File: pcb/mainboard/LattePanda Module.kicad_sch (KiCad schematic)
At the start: 12 parts, among them J1 Conn_01x03_Pin

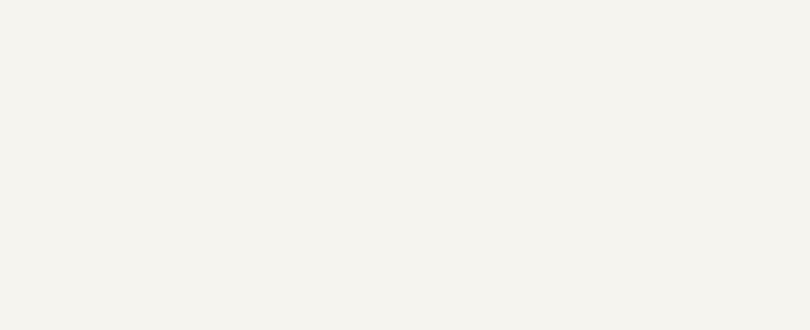
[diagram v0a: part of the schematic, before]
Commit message: most length matching almost done
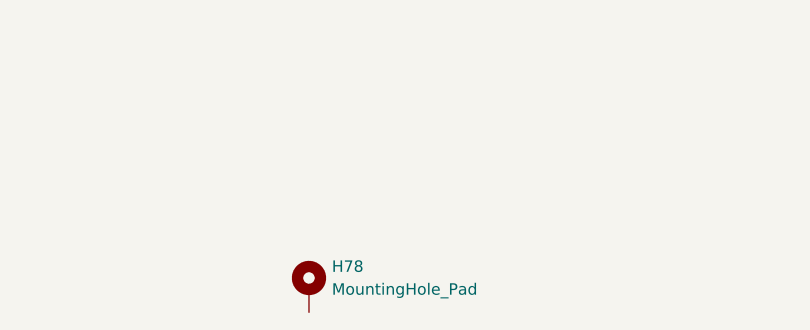
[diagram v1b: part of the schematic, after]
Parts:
- added H78: MountingHole_Pad, A_HDJ_Library:MountingHole_3mm_M2_Pad_TopOnly, symbol Mechanical:MountingHole_Pad
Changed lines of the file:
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@@
+	)
+	(symbol
+		(lib_name "MountingHole_Pad_1")
+		(lib_id "Mechanical:MountingHole_Pad")
+		(at 154.94 346.71 0)
+		(unit 1)
+		(exclude_from_sim no)
+		(in_bom no)
+		(on_board yes)
+		(dnp no)
+		(fields_autoplaced yes)
+		(property "Reference" "H78"
+			(at 157.48 344.1699 0)
+			(effects
+				(font
+					(size 1.27 1.27)
+				)
+				(justify left)
+			)
+		)
+		(property "Value" "MountingHole_Pad"
+			(at 157.48 346.7099 0)
+			(effects
+				(font
+					(size 1.27 1.27)
+				)
+				(justify left)
+			)
+		)
+		(property "Footprint" "A_HDJ_Library:MountingHole_3mm_M2_Pad_TopOnly"
+			(at 154.94 346.71 0)
+			(effects
+				(font
+					(size 1.27 1.27)
+				)
+				(hide yes)
+			)
+		)
+		(property "Datasheet" "~"
+			(at 154.94 346.71 0)
+			(effects
+				(font
+					(size 1.27 1.27)
+				)
+				(hide yes)
+			)
+		)
+		(property "Description" "Mounting Hole with connection"
+			(at 154.94 346.71 0)
+			(effects
+				(font
+					(size 1.27 1.27)
+				)
+				(hide yes)
+			)
+		)
+		(pin "1"
+		)
+		(instances
+			(project ""
+				(path "/2a6d114a-7fd7-4207-b5f7-4ea9c34f36aa/6eee02c2-78c9-4e83-9ccf-e0f7690b57bf"
+					(reference "H78")
+					(unit 1)
+				)
+			)
+		)
 	)
 	(symbol
